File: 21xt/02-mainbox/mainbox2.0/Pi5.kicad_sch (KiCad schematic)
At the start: 4 parts, among them J12 Conn_02x20_Odd_Even

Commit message: schematic check
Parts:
- added C14, C15: 0.1uF, symbol Device:C
- added IC1: SN74LVC2T45DCTTG4, symbol Logic_LevelTranslator:SN74LVC2T45DCTTG4
- added J1, J8: Conn_01x03, symbol Connector_Generic:Conn_01x03
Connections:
- net 3V3: now also C14.2, IC1.8 (VCCB)
- net GND: now also C14.1, C15.1, IC1.4 (GND), IC1.5 (DIR), J1.1 (Pin_1), J8.3 (Pin_3)
- net DO4 renamed IN1(3.3V)
- net IN1(3.3V): now also IC1.7 (B1)
- net DO5 renamed IN2(3.3V)
- net IN2(3.3V): now also IC1.6 (B2)
- net DO6: no longer names the net of J12.15 (Pin_15)
- new net: C15.2, IC1.1 (VCCA)
- new net IN1(5V): IC1.2 (A1), J1.3 (Pin_3)
- new net IN2(5V): IC1.3 (A2), J1.2 (Pin_2)
- new net NAVIN: J8.2 (Pin_2)
- new net NAVOUT: J8.1 (Pin_1)
- no-connect marks 23 -> 24
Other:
- moved on the sheet: J12, R10, R8, R9

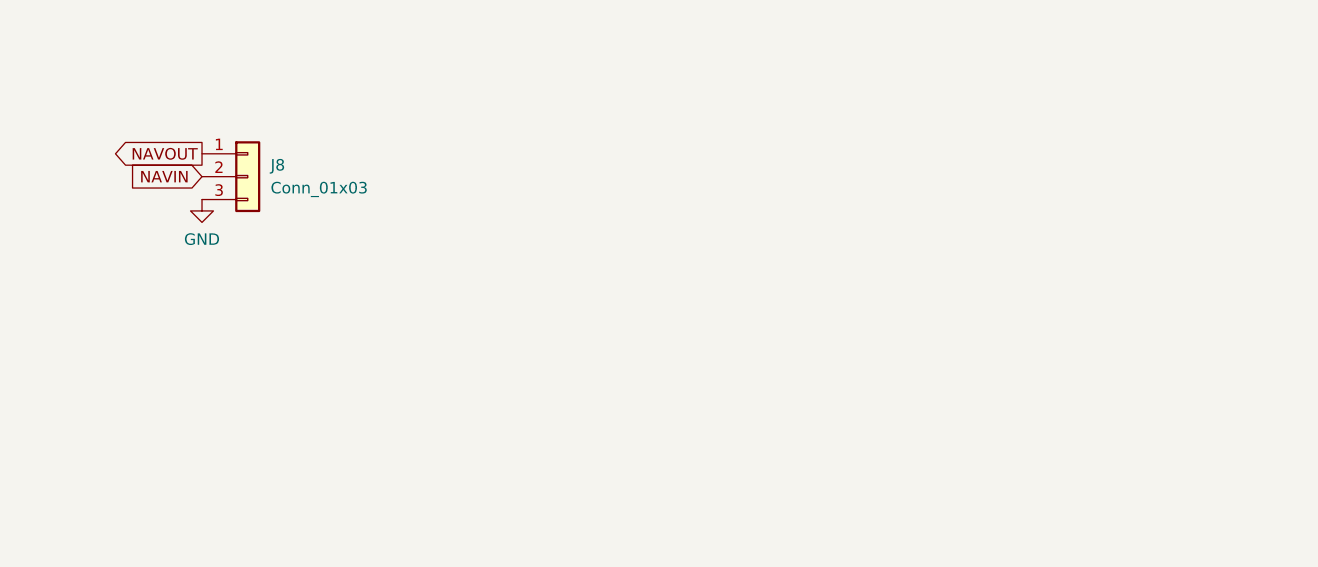
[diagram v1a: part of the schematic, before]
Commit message: schematic markups minus pcie
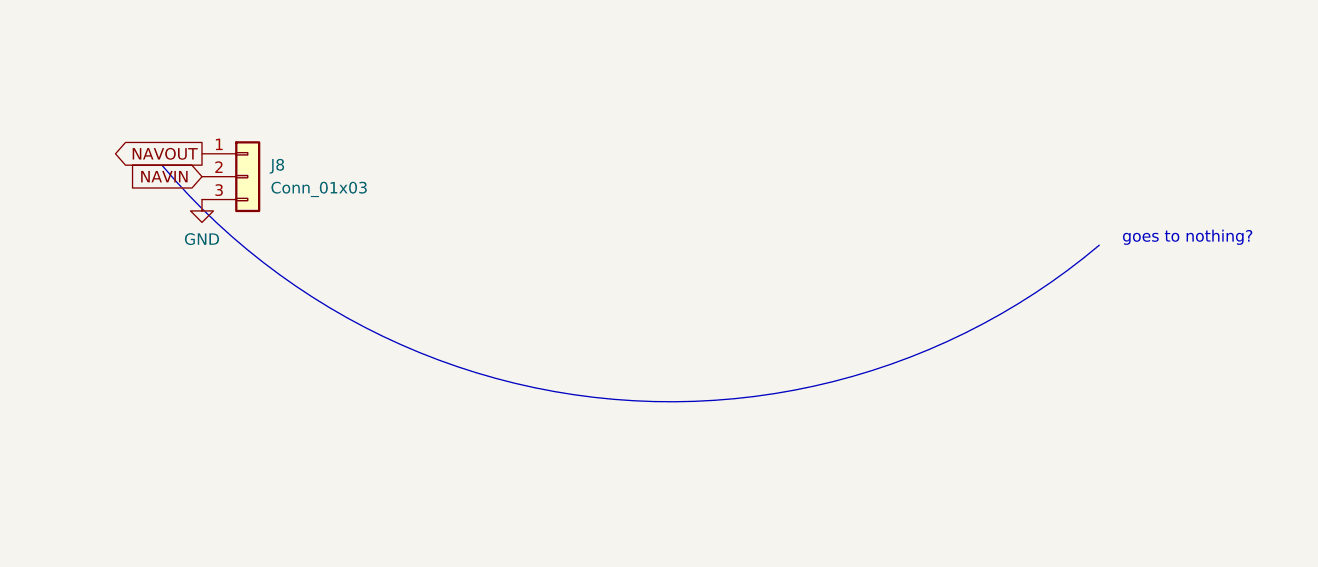
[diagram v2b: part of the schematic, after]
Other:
- note added: "goes to nothing?"
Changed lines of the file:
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@@
     (stroke (width 0) (type default))
+  )
+  (arc (start 313.69 99.06) (mid 259.7788 116.1831) (end 209.55 90.17)
+    (stroke (width 0) (type default))
+    (fill (type none))
+  )
+  (text "goes to nothing?" (at 316.23 99.06 0)
+    (effects (font (size 1.27 1.27)) (justify left bottom))
   )
   (global_label "DO2" (shape input) (at 130.81 101.6 180) (fields_autoplaced)
@@
     (instances
       (project "mainbox2.0"
-        (path "/f7ca7218-80bf-4776-ba9d-a28b83375023/bf2c5ac3-2669-4246-9310-6950262cb4f7"
-          (reference "IC1") (unit 1)
-        )
         (path "/f7ca7218-80bf-4776-ba9d-a28b83375023/207b5b12-0ce1-4f26-8b0d-1e52ecb6d10e"
           (reference "IC1") (unit 1)

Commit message: pcie comments
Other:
- note added: "??? what are these"
- note added: "also if these are wheel speed sensors then the in 5v should be where the signals are being generated and the 3v3 is where the translator should be sent"
- note added: "im not sure it can comprehend unidurectional unless you have completely isolated levels but not 100%"
- note added: "make these tags more descriptive"
- note added: "missing h bridge pwm + enables"
- note added: "missing serial line for power ;board"
- note added: "missing steering wheel uart"
- note added: "need to swap the dir pin to match opposite direction or just swap 5v 3v sides"
- note added: "tag direction"

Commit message: progress
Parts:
- removed J1, J8: Conn_01x03, symbol Connector_Generic:Conn_01x03
- added J1: Conn_01x10, 21xt_footprints:908160010(picolex-10), symbol Connector_Generic:Conn_01x10
- C14, C15: footprint (none) -> Capacitor_SMD:C_0603_1608Metric
- IC1: footprint (none) -> 21xt_footprints:SOP65P400X130-8N
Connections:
- net CS is gone; now on net NAVIN: J12.24 (Pin_24)
- net 5.2V: now also C15.2, IC1.1 (VCCA), J1.7 (Pin_7)
- net GND: now also J1.8 (Pin_8)
- net IN1(5V): now also J1.9 (Pin_9)
- net IN2(5V): now also J1.10 (Pin_10)
- net NAVIN: now also J1.2 (Pin_2)
- net NAVOUT: now also J12.28 (Pin_28), J1.1 (Pin_1)
- net SCLK: now also J12.38 (Pin_38); no longer J12.23 (Pin_23)
- net ADC_SPI_DOUT: now reaches J12.12 (Pin_12)
- net STEERING_WHEEL_TX: now reaches J12.27 (Pin_27)
- net STEERING_WHEEL_TX: now also J1.5 (Pin_5)
- net STEERING_WHEEL_RX: now reaches J12.29 (Pin_29)
- net STEERING_WHEEL_RX: now also J1.6 (Pin_6)
- net ADC_SPI_DIN: now reaches J12.35 (Pin_35)
- net RPi_SPI_CS: now reaches J12.36 (Pin_36)
- net DIN: no longer names the net of J12.19 (Pin_19)
- net DO1 renamed DIGITAL_OUTPUT_1
- net DO2 renamed DIGITAL_OUTPUT_2
- net DO3 renamed POWER_BOARD_RX
- net POWER_BOARD_RX: now also J1.4 (Pin_4)
- net DOUT renamed POWER_BOARD_TX
- net POWER_BOARD_TX: now also J1.3 (Pin_3)
- no-connect marks 24 -> 17
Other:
- note added: "https://pinout.xyz/pinout/uart : my reference"
- note removed: "??? what are these"
- note removed: "also if these are wheel speed sensors then the in 5v should be where the signals are being generated and the 3v3 is where the translator should be sent"
- note removed: "im not sure it can comprehend unidurectional unless you have completely isolated levels but not 100%"
- note removed: "make these tags more descriptive"
- note removed: "missing h bridge pwm + enables"
- note removed: "missing serial line for power ;board"
- note removed: "missing steering wheel uart"
- note removed: "need to swap the dir pin to match opposite direction or just swap 5v 3v sides"
- note removed: "tag direction"
- moved on the sheet: J12, R10, R8, R9
